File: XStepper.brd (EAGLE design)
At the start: 100.3 x 80 mm, 75 parts, among them IC2 7812TV, Q2 16 MHZ

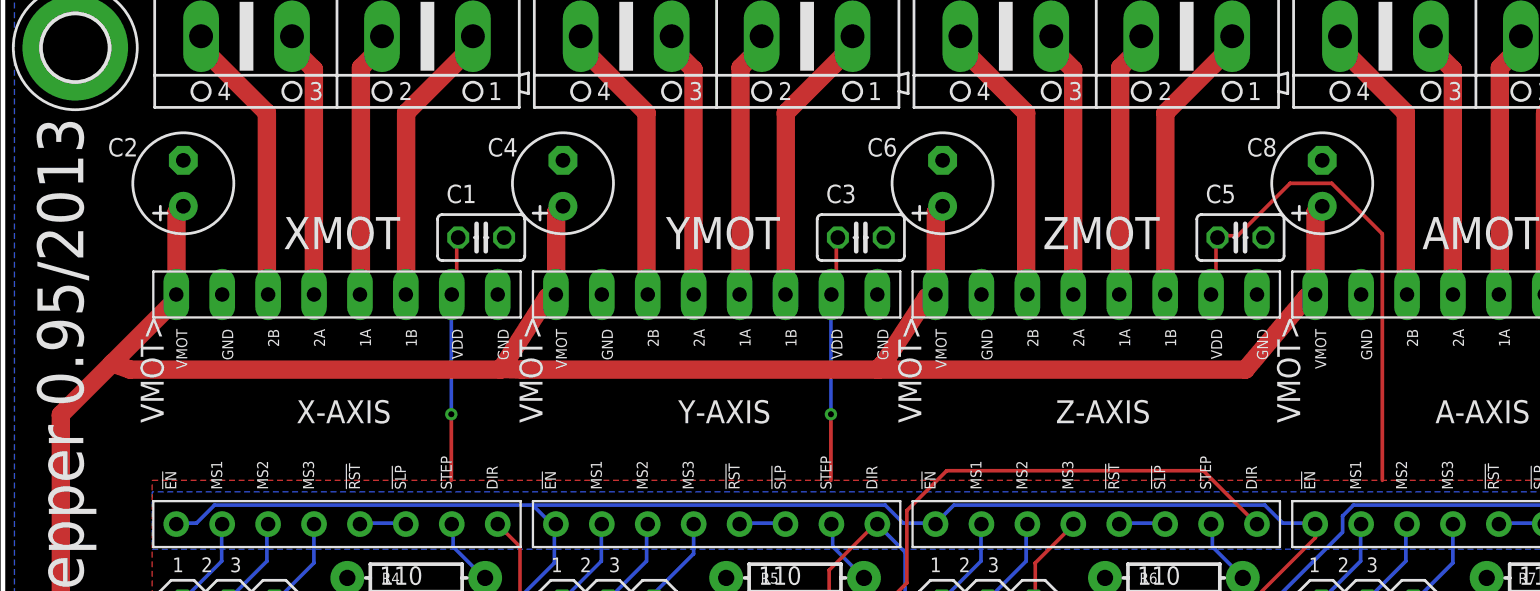
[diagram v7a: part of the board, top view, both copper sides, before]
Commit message: - bigger vmot caps 8mm
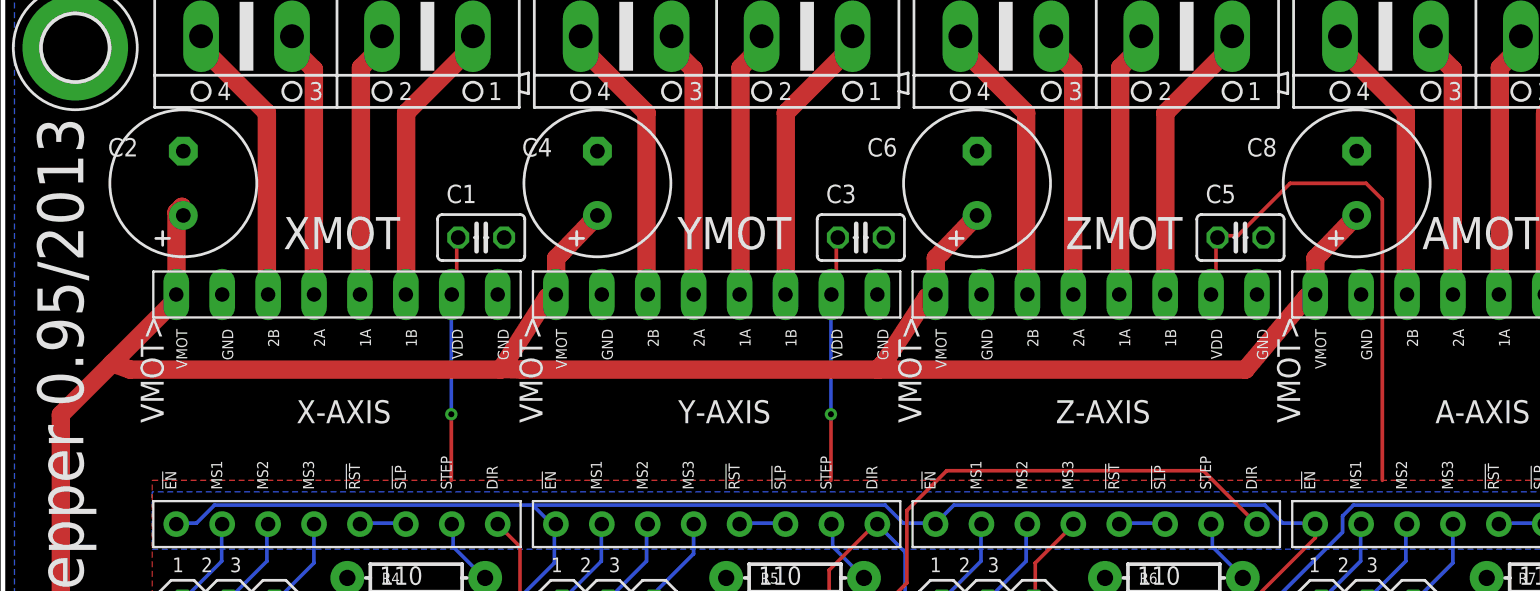
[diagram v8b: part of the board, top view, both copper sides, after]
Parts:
- C2, C4, C6, C8: device resistor:E2,5-6 -> resistor:E3,5-8
- moved C4 1.91 mm to (32.9, 68.5)
- moved C6 1.91 mm to (53.9, 68.5)
- moved C8 1.91 mm to (74.9, 68.5)
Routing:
- net 5V: track 69.5 -> 70.6 mm
- net PWRMOT: track 127.9 -> 129.0 mm
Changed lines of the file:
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@@
 <attribute name="VALUE" x="29.6663" y="39.555" size="1.27" layer="27"/>
 </element>
-<element name="C4" library="resistor" package="E2,5-6" value="100uF" x="30.9763" y="68.5" smashed="yes" rot="R90">
-<attribute name="NAME" x="28.4763" y="71" size="1.016" layer="25" font="vector" ratio="10" rot="R180"/>
-<attribute name="VALUE" x="33.6433" y="71.167" size="1.27" layer="27" ratio="10" rot="R90"/>
+<element name="C4" library="resistor" package="E3,5-8" value="100uF" x="32.8813" y="68.5" smashed="yes" rot="R90">
+<attribute name="NAME" x="30.3813" y="71" size="1.016" layer="25" font="vector" ratio="10" rot="R180"/>
+<attribute name="VALUE" x="35.5483" y="71.167" size="1.27" layer="27" ratio="10" rot="R90"/>
 </element>
 <element name="STEPPERDRIVER2" library="pololu-allegro" package="POLOLU-ALLEGRO-PTH" value="POLOLU-A4988" x="60.4763" y="56" smashed="yes" rot="R90"/>
@@
 <attribute name="VALUE" x="50.6663" y="39.555" size="1.27" layer="27"/>
 </element>
-<element name="C6" library="resistor" package="E2,5-6" value="100uF" x="51.9763" y="68.5" smashed="yes" rot="R90">
-<attribute name="VALUE" x="53.7543" y="65.452" size="1.27" layer="27" ratio="10" rot="R180"/>
+<element name="C6" library="resistor" package="E3,5-8" value="100uF" x="53.8813" y="68.5" smashed="yes" rot="R90">
+<attribute name="VALUE" x="55.6593" y="65.452" size="1.27" layer="27" ratio="10" rot="R180"/>
 </element>
 <element name="STEPPERDRIVER3" library="pololu-allegro" package="POLOLU-ALLEGRO-PTH" value="POLOLU-A4988" x="81.4762" y="56" smashed="yes" rot="R90"/>
@@
 <attribute name="VALUE" x="71.6662" y="39.555" size="1.27" layer="27"/>
 </element>
-<element name="C8" library="resistor" package="E2,5-6" value="100uF" x="72.9762" y="68.5" smashed="yes" rot="R90">
-<attribute name="VALUE" x="69.9282" y="66.087" size="1.27" layer="27" ratio="10" rot="R90"/>
+<element name="C8" library="resistor" package="E3,5-8" value="100uF" x="74.8812" y="68.5" smashed="yes" rot="R90">
+<attribute name="VALUE" x="71.8332" y="66.087" size="1.27" layer="27" ratio="10" rot="R90"/>
 </element>
 <element name="C9" library="resistor" package="E2,5-6" value="200uF" x="19.05" y="19.05" smashed="yes" rot="R270">
@@
 <attribute name="MF" value="" x="60.4763" y="76.635" size="1.778" layer="27" rot="R180" display="off"/>
 <attribute name="OC_FARNELL" value="unknown" x="60.4763" y="76.635" size="1.778" layer="27" rot="R180" display="off"/>
-<attribute name="NAME" x="63.9763" y="66.635" size="1.778" layer="25" font="vector" ratio="10" rot="R180"/>
+<attribute name="NAME" x="65.2463" y="66.635" size="1.778" layer="25" font="vector" ratio="10" rot="R180"/>
 <attribute name="VALUE" x="70.5601" y="82.35" size="1.778" layer="27" ratio="10" rot="R180"/>
 </element>
@@
 <attribute name="MF" value="" x="39.4763" y="76.635" size="1.778" layer="27" rot="R180" display="off"/>
 <attribute name="OC_FARNELL" value="unknown" x="39.4763" y="76.635" size="1.778" layer="27" rot="R180" display="off"/>
-<attribute name="NAME" x="42.9763" y="66.635" size="1.778" layer="25" font="vector" ratio="10" rot="R180"/>
+<attribute name="NAME" x="43.6113" y="66.635" size="1.778" layer="25" font="vector" ratio="10" rot="R180"/>
 <attribute name="VALUE" x="49.5601" y="82.35" size="1.778" layer="27" ratio="10" rot="R180"/>
 </element>
@@
 <attribute name="VALUE" x="91.7385" y="68.294" size="1.27" layer="27" ratio="10" rot="R180"/>
 </element>
-<element name="C2" library="resistor" package="E2,5-6" value="100uF" x="9.9763" y="68.5" smashed="yes" rot="R90">
+<element name="C2" library="resistor" package="E3,5-8" value="100uF" x="9.9763" y="68.5" smashed="yes" rot="R90">
 <attribute name="NAME" x="7.4763" y="71" size="1.016" layer="25" font="vector" ratio="10" rot="R180"/>
 <attribute name="VALUE" x="12.6433" y="71.167" size="1.27" layer="27" ratio="10" rot="R90"/>
@@
 <wire x1="68.3" y1="65.6" x2="67.2" y2="65.6" width="0.2032" layer="1"/>
 <wire x1="71.2" y1="68.5" x2="68.3" y2="65.6" width="0.2032" layer="1"/>
-<wire x1="73.5" y1="68.5" x2="71.2" y2="68.5" width="0.2032" layer="1"/>
-<wire x1="76.3" y1="65.7" x2="73.5" y2="68.5" width="0.2032" layer="1"/>
-<wire x1="76.3" y1="52.07" x2="76.3" y2="65.7" width="0.2032" layer="1"/>
+<wire x1="75.405" y1="68.5" x2="71.2" y2="68.5" width="0.2032" layer="1"/>
+<wire x1="76.3" y1="67.605" x2="75.405" y2="68.5" width="0.2032" layer="1"/>
+<wire x1="76.3" y1="52.07" x2="76.3" y2="67.605" width="0.2032" layer="1"/>
 <wire x1="67.2" y1="65.6" x2="67.1825" y2="65.5" width="0.2032" layer="1"/>
 <wire x1="87.9" y1="52.07" x2="87.9" y2="62.3" width="0.2032" layer="1"/>
@@
 <contactref element="C8" pad="+"/>
 <contactref element="C2" pad="+"/>
-<wire x1="72.6" y1="66.9" x2="72.6" y2="62.4" width="1.016" layer="1"/>
-<wire x1="72.9" y1="67.2" x2="72.6" y2="66.9" width="1.016" layer="1"/>
+<wire x1="72.6" y1="64.36" x2="72.6" y2="62.4" width="1.016" layer="1"/>
+<wire x1="72.9" y1="64.66" x2="72.6" y2="64.36" width="1.016" layer="1"/>
 <wire x1="72.6" y1="62.4" x2="72.5862" y2="62.35" width="1.016" layer="1"/>
-<wire x1="72.9" y1="67.2" x2="72.9762" y2="67.23" width="1.016" layer="1"/>
-<wire x1="51.6" y1="66.9" x2="51.6" y2="62.4" width="1.016" layer="1"/>
-<wire x1="51.9" y1="67.2" x2="51.6" y2="66.9" width="1.016" layer="1"/>
+<wire x1="72.9" y1="64.66" x2="74.8812" y2="66.722" width="1.016" layer="1"/>
+<wire x1="51.6" y1="64.36" x2="51.6" y2="62.4" width="1.016" layer="1"/>
+<wire x1="51.9" y1="64.66" x2="51.6" y2="64.36" width="1.016" layer="1"/>
 <wire x1="51.6" y1="62.4" x2="51.5863" y2="62.35" width="1.016" layer="1"/>
-<wire x1="51.9" y1="67.2" x2="51.9763" y2="67.23" width="1.016" layer="1"/>
-<wire x1="30.6" y1="66.9" x2="30.6" y2="62.4" width="1.016" layer="1"/>
-<wire x1="30.9" y1="67.2" x2="30.6" y2="66.9" width="1.016" layer="1"/>
+<wire x1="51.9" y1="64.66" x2="53.8813" y2="66.722" width="1.016" layer="1"/>
+<wire x1="30.6" y1="64.36" x2="30.6" y2="62.4" width="1.016" layer="1"/>
+<wire x1="30.9" y1="64.66" x2="30.6" y2="64.36" width="1.016" layer="1"/>
 <wire x1="30.6" y1="62.4" x2="30.5863" y2="62.35" width="1.016" layer="1"/>
-<wire x1="30.9" y1="67.2" x2="30.9763" y2="67.23" width="1.016" layer="1"/>
+<wire x1="30.9" y1="64.66" x2="32.8813" y2="66.722" width="1.016" layer="1"/>
 <wire x1="9.6" y1="66.9" x2="9.6" y2="62.4" width="1.016" layer="1"/>
 <wire x1="9.9" y1="67.2" x2="9.6" y2="66.9" width="1.016" layer="1"/>
 <wire x1="9.6" y1="62.4" x2="9.5863" y2="62.35" width="1.016" layer="1"/>
-<wire x1="9.9" y1="67.2" x2="9.9763" y2="67.23" width="1.016" layer="1"/>
+<wire x1="9.9" y1="67.2" x2="9.9763" y2="66.722" width="1.016" layer="1"/>
 <wire x1="3.2" y1="55.7" x2="3.2" y2="36.9" width="1.016" layer="1"/>
 <wire x1="9.4" y1="61.9" x2="6.045" y2="58.545" width="1.016" layer="1"/>
@@
 </signal>
 </signals>
-<errors>
-</errors>
 </board>
 </drawing>
